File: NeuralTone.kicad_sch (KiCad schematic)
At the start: 90 parts, among them J1 USB-C PD, J2 Guitar, J3 Headphones, J4 USB-A Port, J5 Line Out, J6 5V Fan, J7 TF-01A, Q1 AON7421, Q2 IRLML6344, SW1 SW_Push, U1 AP2125N-3.3, U2 CH224K, U3 MCP6022, U4 AP2125N-3.3, U5 AP2151, U6 NAU8814YG, U7 DRTR5V0U2SR, Y1 OT322512MJBA4SL

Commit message: stop worrying about coupling caps and be done with it
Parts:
- C16: value 470u -> 1000u; LCSC C251022 -> C178587
- C24, C5: footprint Capacitor_SMD:CP_Elec_4x5.3 -> Capacitor_SMD:CP_Elec_4x5.7; LCSC C2163079 -> C242076
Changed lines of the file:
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@@
       (effects (font (size 1.27 1.27)))
     )
-    (property "Footprint" "Capacitor_SMD:CP_Elec_4x5.3" (at 292.735 60.96 0)
+    (property "Footprint" "Capacitor_SMD:CP_Elec_4x5.7" (at 292.735 60.96 0)
       (effects (font (size 1.27 1.27)) hide)
     )
@@
       (effects (font (size 1.27 1.27)) hide)
     )
-    (property "LCSC" "C2163079" (at 292.735 60.96 90)
+    (property "LCSC" "C242076" (at 292.735 60.96 90)
       (effects (font (size 1.27 1.27)) hide)
     )
@@
       (effects (font (size 1.27 1.27)))
     )
-    (property "Value" "470u" (at 233.68 142.24 90)
+    (property "Value" "1000u" (at 233.68 142.24 90)
       (effects (font (size 1.27 1.27)))
     )
@@
       (effects (font (size 1.27 1.27)) hide)
     )
-    (property "LCSC" "C251022" (at 233.68 136.525 90)
+    (property "LCSC" "C178587" (at 233.68 136.525 90)
       (effects (font (size 1.27 1.27)) hide)
     )
@@
       (effects (font (size 1.27 1.27)))
     )
-    (property "Footprint" "Capacitor_SMD:CP_Elec_4x5.3" (at 233.68 163.195 0)
+    (property "Footprint" "Capacitor_SMD:CP_Elec_4x5.7" (at 233.68 163.195 0)
       (effects (font (size 1.27 1.27)) hide)
     )
@@
       (effects (font (size 1.27 1.27)) hide)
     )
-    (property "LCSC" "C2163079" (at 233.68 163.195 90)
-      (effects (font (size 1.27 1.27)) hide)
-    )
+    (property "LCSC" "C242076" (at 233.68 163.195 90)
+      (effects (font (size 1.27 1.27)) hide)
+    )

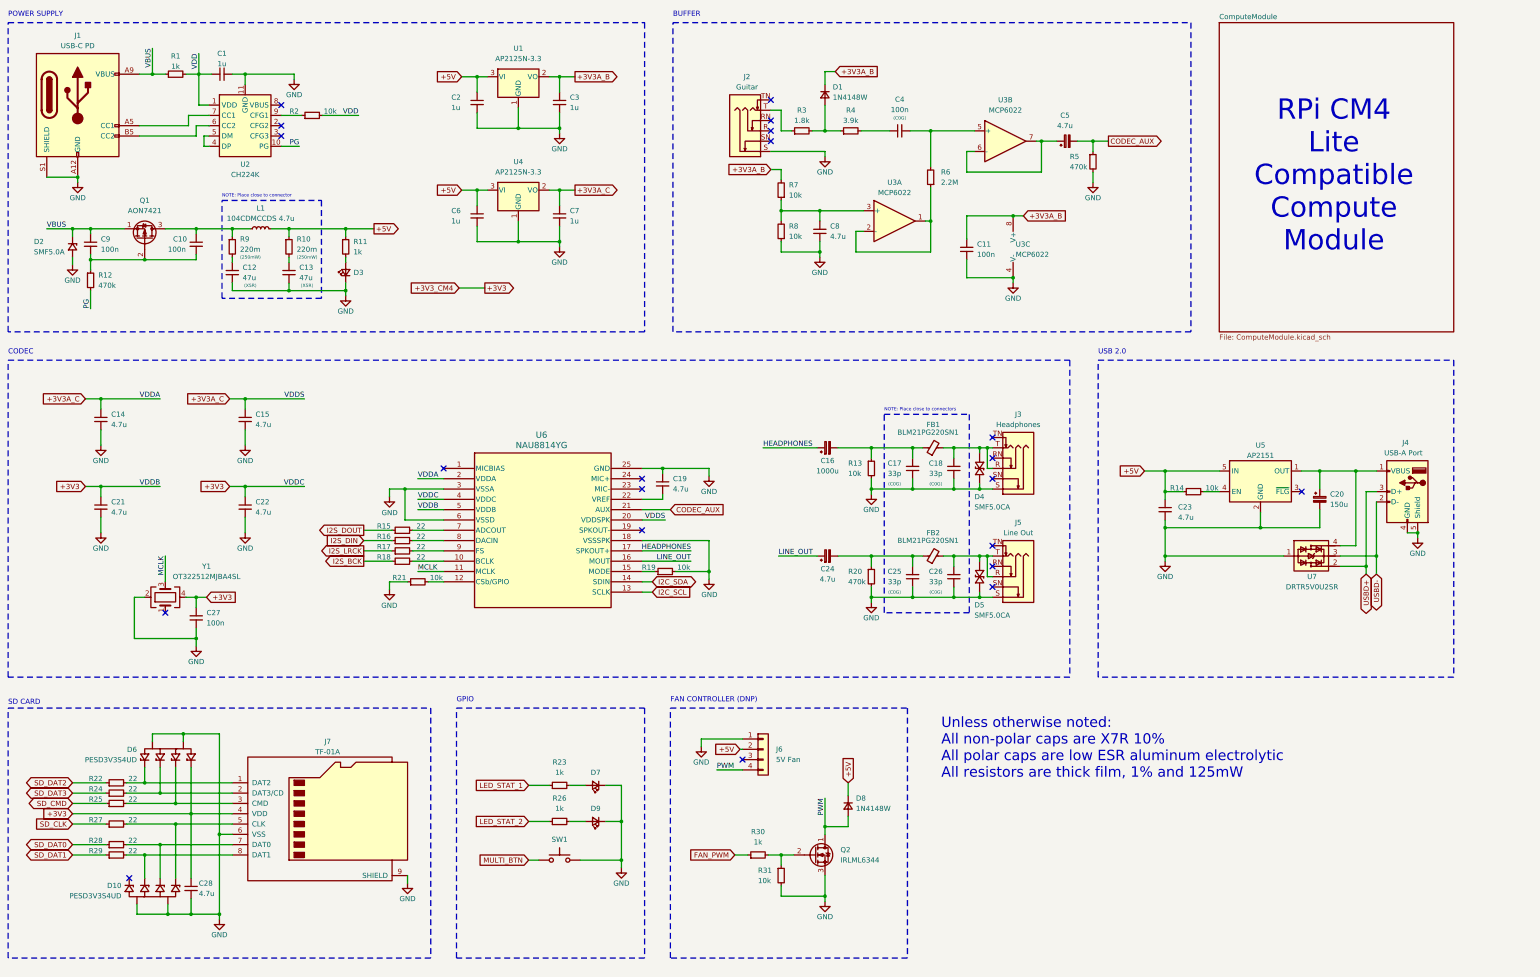
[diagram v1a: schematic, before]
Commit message: more power for output, bigger cap
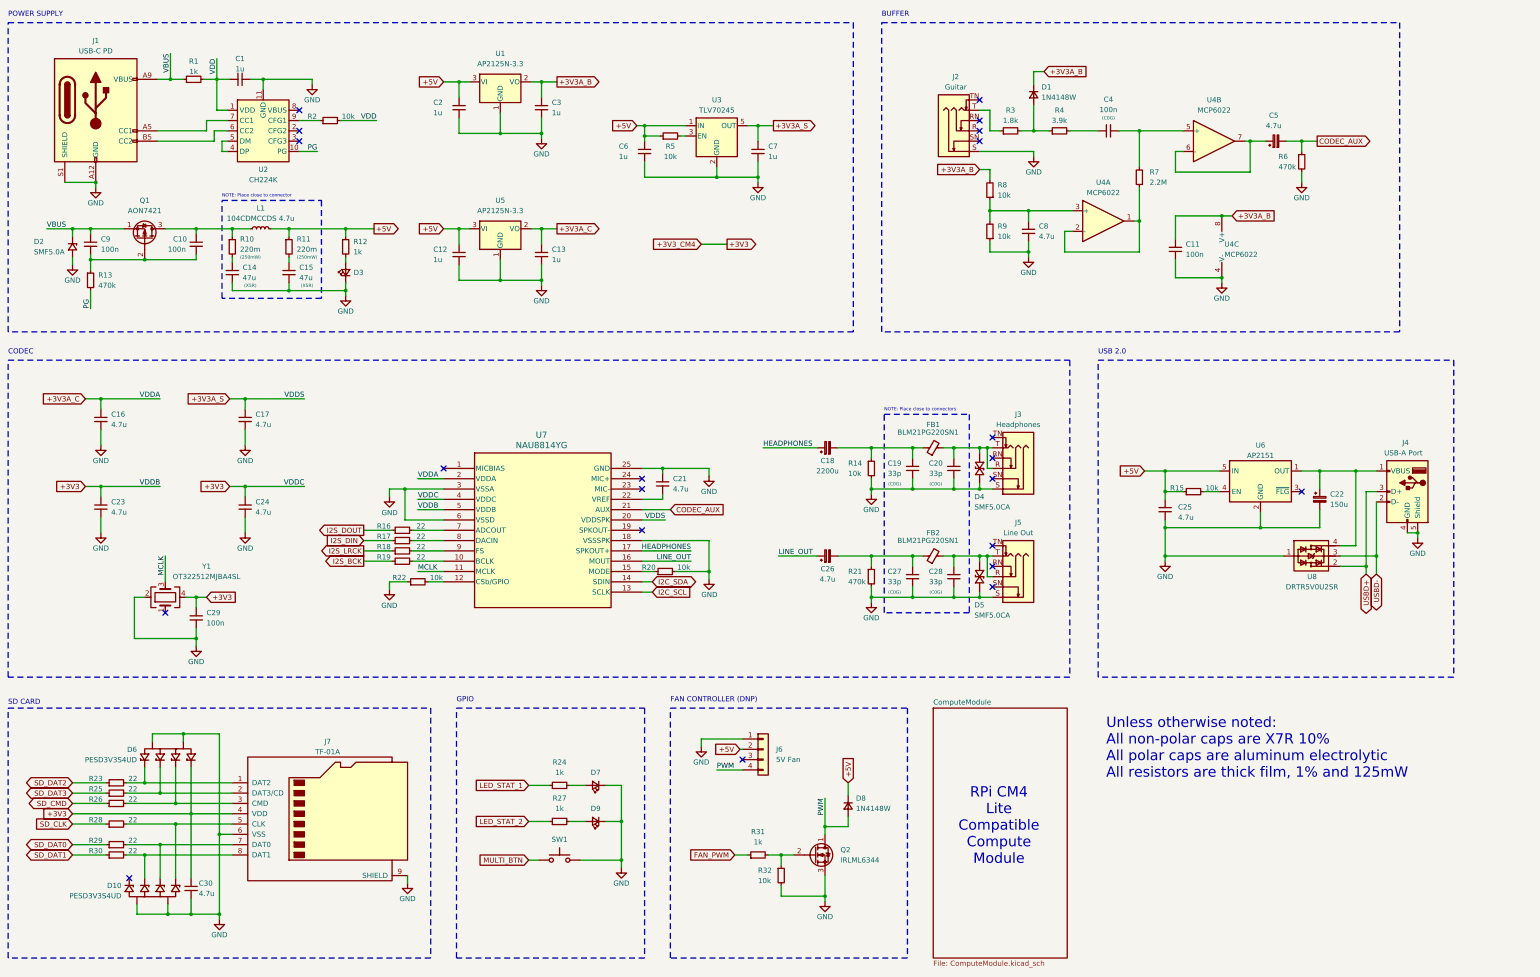
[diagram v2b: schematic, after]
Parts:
- added C6, C7: 1u, Capacitor_SMD:C_0805_2012Metric_Pad1.18x1.45mm_HandSolder, symbol Device:C_Small
- added R5: 10k, Resistor_SMD:R_0805_2012Metric_Pad1.20x1.40mm_HandSolder, symbol Device:R_Small
- added U3: TLV70245, Package_TO_SOT_SMD:SOT-23-5, symbol Regulator_Linear:TLV70245_SOT23-5
- C18: renamed from C16; value 1000u -> 2200u; LCSC C178587 -> C401762
- renumbered C6 to C12, C7 to C13, C12 to C14, C13 to C15, C14 to C16, C15 to C17, C17 to C19, C18 to C20, C19 to C21, C20 to C22, C21 to C23, C22 to C24, C23 to C25, C24 to C26, C25 to C27, C26 to C28, C27 to C29, C28 to C30, R9 to R10, R10 to R11, R11 to R12, R12 to R13, R13 to R14, R14 to R15, R15 to R16, R16 to R17, R17 to R18, R18 to R19, R19 to R20, R20 to R21, R21 to R22, R22 to R23, R23 to R24, R24 to R25, R25 to R26, R26 to R27, R27 to R28, R28 to R29, R29 to R30, R30 to R31, R31 to R32, R5 to R6, R6 to R7, R7 to R8, R8 to R9, U3 to U4, U4 to U5, U5 to U6, U6 to U7, U7 to U8
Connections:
- net +3V3A_C: no longer C17.1, U7.20 (VDDSPK)
- net +5V: now also C6.1, R5.1, U3.1 (IN)
- net GND: now also C6.2, C7.2, U3.2 (GND)
- new net: R5.2, U3.3 (EN)
- new net +3V3A_S: C17.1, C7.1, U3.5 (OUT), U7.20 (VDDSPK)
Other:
- moved on the sheet: C1, C11, C12, C13, C2, C3, C4, C5, C8, D1, J1, J2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

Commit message: fix speaker voltage and current switch diode
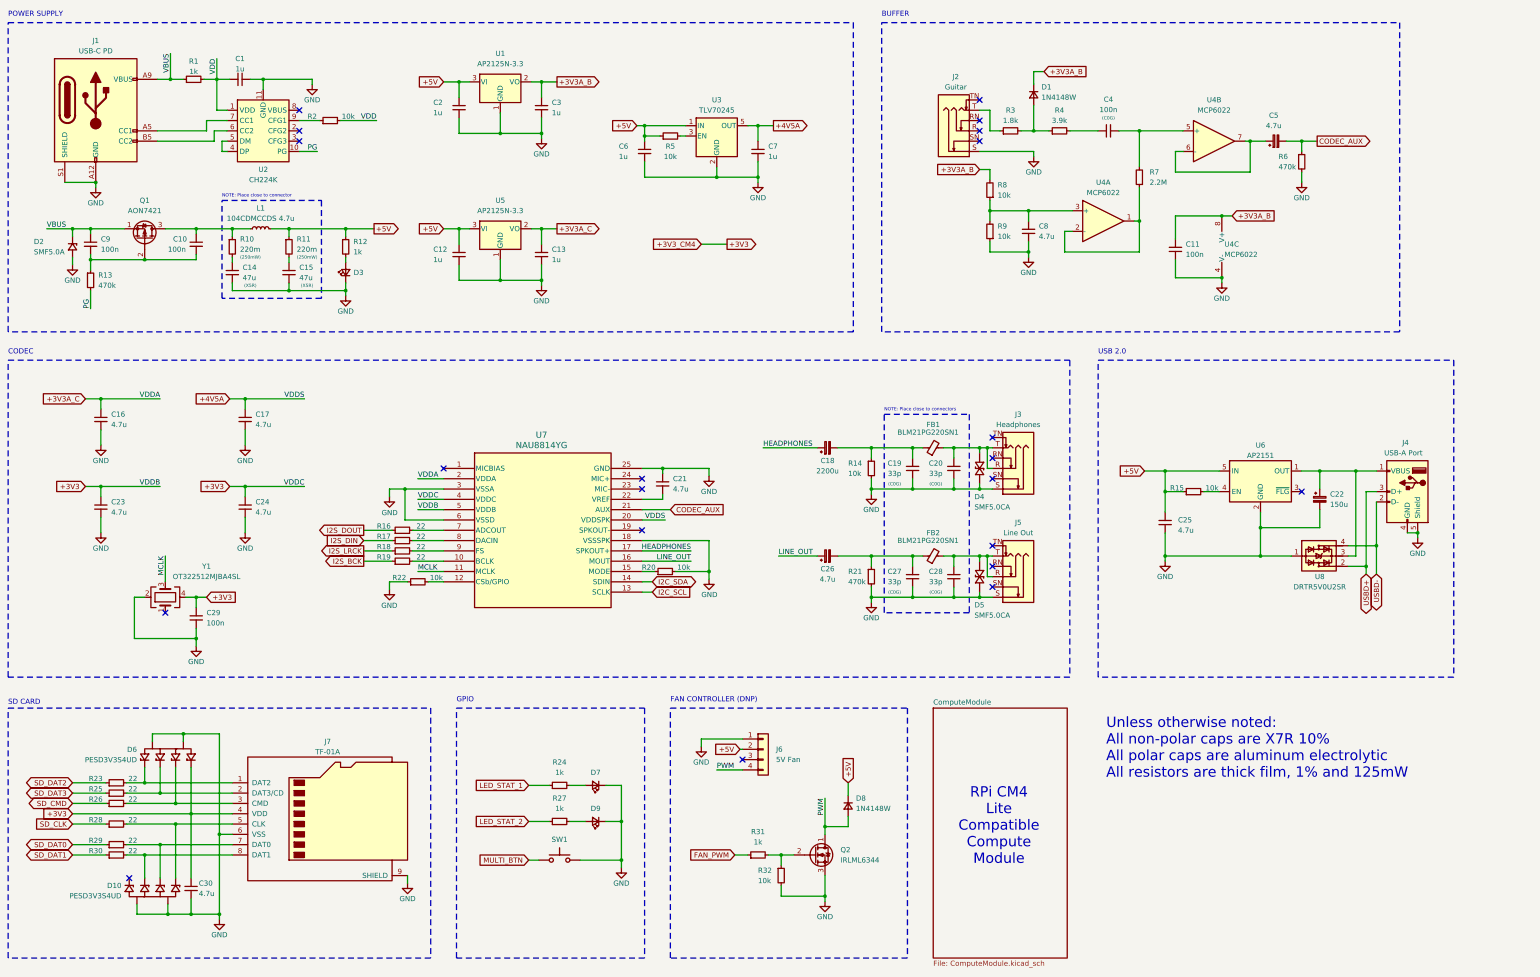
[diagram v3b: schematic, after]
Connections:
- net USBD-: now also U8.4; no longer U8.3
- net at C22.1, J4.1 (VBUS), U6.1 (OUT): now also U8.3; no longer U8.4
- net +3V3A_S renamed +4V5A
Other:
- moved on the sheet: C25, U8

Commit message: switch power to 9V
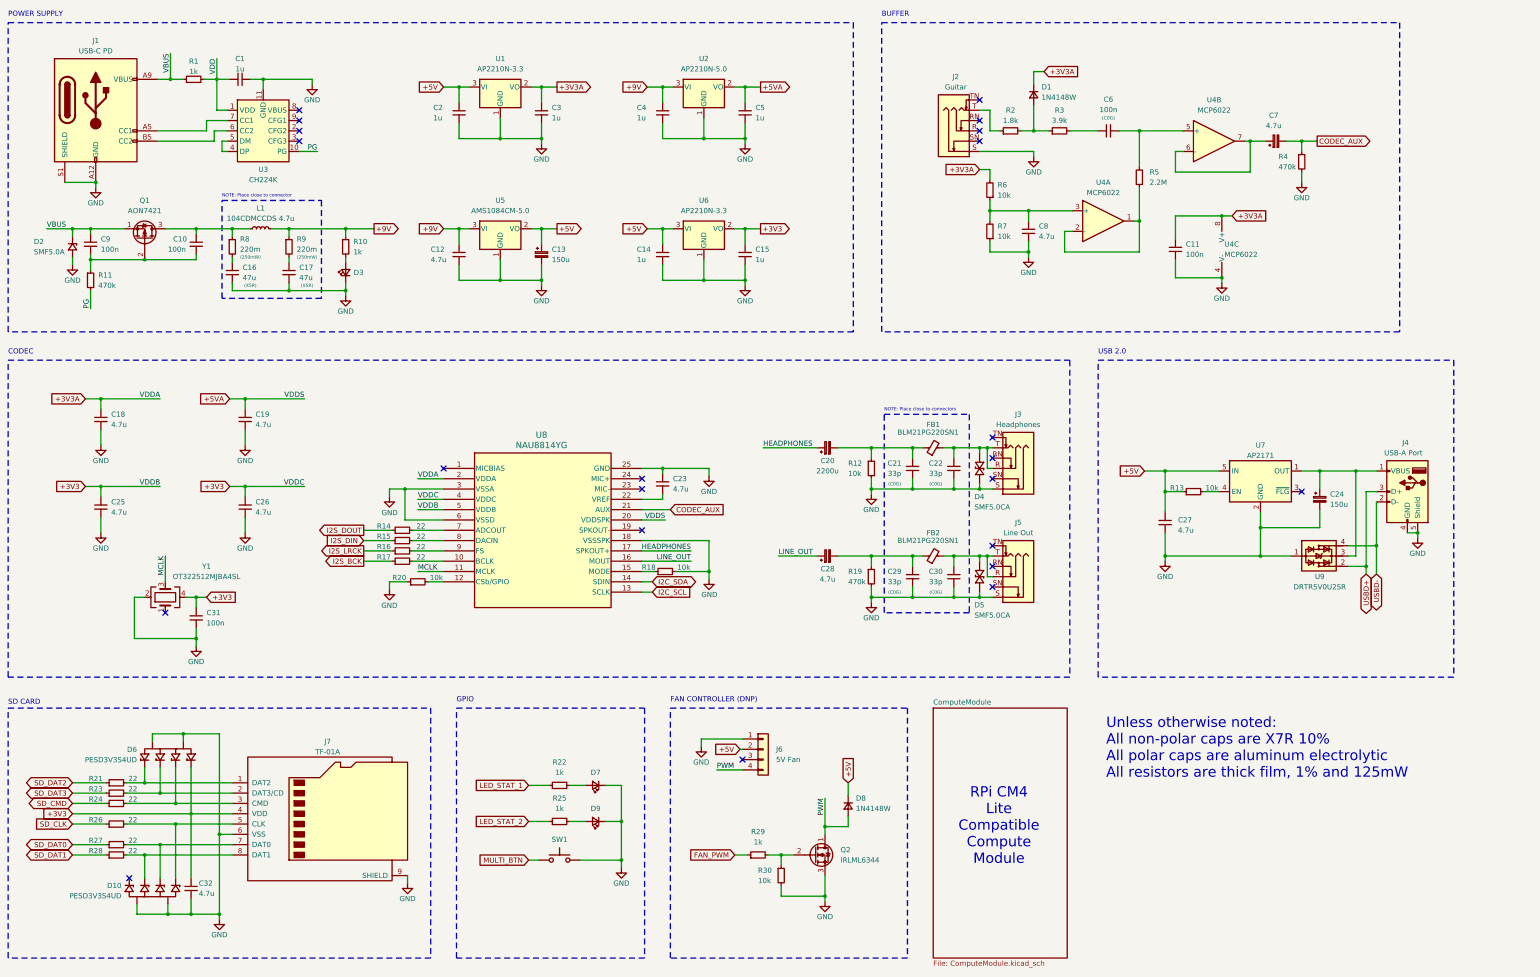
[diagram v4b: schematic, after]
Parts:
- removed C6, C7: 1u, Capacitor_SMD:C_0805_2012Metric_Pad1.18x1.45mm_HandSolder, symbol Device:C_Small
- removed R2, R5: 10k, Resistor_SMD:R_0805_2012Metric_Pad1.20x1.40mm_HandSolder, symbol Device:R_Small
- removed U3: TLV70245, Package_TO_SOT_SMD:SOT-23-5, symbol Regulator_Linear:TLV70245_SOT23-5
- added C12: 4.7u, Capacitor_SMD:C_0805_2012Metric_Pad1.18x1.45mm_HandSolder, symbol Device:C_Small
- added C13: 150u, Capacitor_SMD:CP_Elec_6.3x7.7, symbol Device:C_Polarized_Small
- added C4, C5: 1u, Capacitor_SMD:C_0805_2012Metric_Pad1.18x1.45mm_HandSolder, symbol Device:C_Small
- added U2: AP2210N-5.0, Package_TO_SOT_SMD:SOT-23, symbol Regulator_Linear:AP2127N-3.3
- added U6: AP2210N-3.3, Package_TO_SOT_SMD:SOT-23, symbol Regulator_Linear:AP2127N-3.3
- U1: value AP2125N-3.3 -> AP2210N-3.3; LCSC C150715 -> C460341
- U5: value AP2125N-3.3 -> AMS1084CM-5.0; footprint Package_TO_SOT_SMD:SOT-23 -> Package_TO_SOT_SMD:TO-263-3_TabPin2; LCSC C150715 -> C56105
- U7: renamed from U6; value AP2151 -> AP2171; LCSC C110464 -> C110466
- U8: renamed from U7; footprint Package_DFN_QFN:QFN-24-1EP_4x4mm_P0.5mm_EP2.6x2.6mm_ThermalVias -> NeuralTone:QFN-24_4X4_NUV-M
- renumbered C12 to C14, C13 to C15, C14 to C16, C15 to C17, C16 to C18, C17 to C19, C18 to C20, C19 to C21, C20 to C22, C21 to C23, C22 to C24, C23 to C25, C24 to C26, C25 to C27, C26 to C28, C27 to C29, C28 to C30, C29 to C31, C30 to C32, C4 to C6, C5 to C7, R12 to R10, R13 to R11, R14 to R12, R15 to R13, R16 to R14, R17 to R15, R18 to R16, R19 to R17, R20 to R18, R21 to R19, R3 to R2, R22 to R20, R23 to R21, R24 to R22, R25 to R23, R26 to R24, R27 to R25, R28 to R26, R29 to R27, R30 to R28, R31 to R29, R4 to R3, R32 to R30, R6 to R4, R7 to R5, R8 to R6, R9 to R7, R10 to R8, R11 to R9, U2 to U3, U8 to U9
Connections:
- net +3V3: now also C15.1, U6.2 (VO)
- net +5V: now also U5.2 (VO), C13.1, U6.3 (VI); no longer L1.2, R10.1, R9.1, U5.3 (VI)
- net GND: now also C12.2, C13.2, C4.2, C5.2, U2.1 (GND), U6.1 (GND)
- net +3V3A_B renamed +3V3A
- net +3V3A: now also C18.1, U8.2 (VDDA)
- removed net +3V3A_C: C15.1, C18.1, U5.2 (VO), U8.2 (VDDA)
- net +4V5A renamed +5VA
- net +5VA: now also C5.1, U2.2 (VO)
- new net +9V: C12.1, C4.1, L1.2, R10.1, R9.1, U2.3 (VI), U5.3 (VI)
- no-connect marks 21 -> 22
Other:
- moved on the sheet: C14, C15, C2, C3, U1

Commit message: fine tuning before layout
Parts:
- removed C12, C27: 4.7u, Capacitor_SMD:C_0805_2012Metric_Pad1.18x1.45mm_HandSolder, symbol Device:C_Small
- added C12, C25: 10u, Capacitor_SMD:CP_Elec_4x5.8, symbol Device:C_Polarized_Small
- C28, C7: value 4.7u -> 10u; footprint Capacitor_SMD:CP_Elec_4x5.7 -> Capacitor_SMD:CP_Elec_4x5.8; LCSC C242076 -> C401709
- D2: value SMF5.0A -> SMF9.0A; LCSC C2905637 -> C5270738
- L1: value 104CDMCCDS 4.7u -> 0412CDMCCDS-R10MC; LCSC C167296 -> C2595939
- R7: renamed from R8; value 220m -> 100m; LCSC C25336 -> C858723
- R8: renamed from R9; value 220m -> 100m; LCSC C25336 -> C858723
- renumbered C8 to C10, C25 to C26, C26 to C27, C9 to C8, C10 to C9, R7 to R10, R10 to R9
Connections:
- net +5V: now also C25.1
- net +9V: now also C12.1
- net GND: now also C12.2, C25.2
- net +3V3 renamed +3.3V
- net +3V3A renamed +3.3VA
- net VDD: no longer names the net of C1.2, R1.2, U3.1 (VDD)
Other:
- moved on the sheet: C10, C18, C19, C26, C27, C31, J6, R10, R4, R5, R6, U4A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
